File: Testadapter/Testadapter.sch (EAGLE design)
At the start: 47 parts, among them T1 C8492, T2 C8492, T3 C8545, T4 C8545, X1 MKDSN1,5/2-5,08

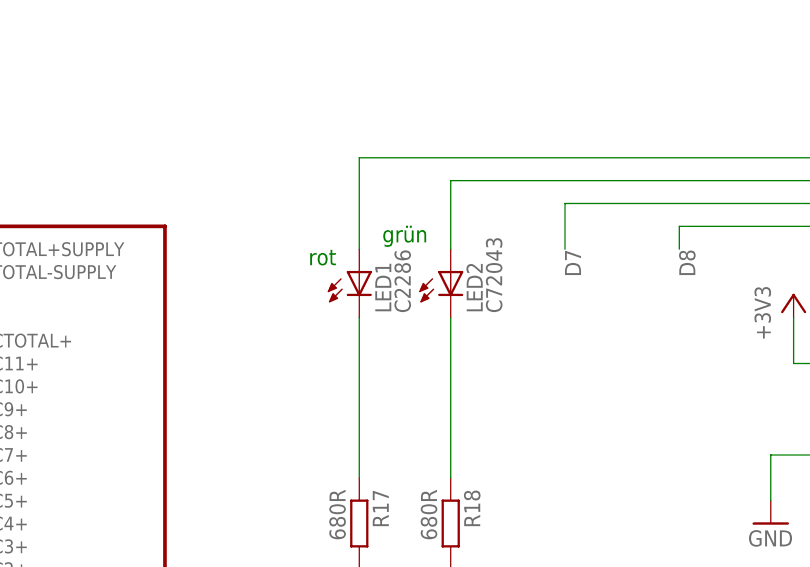
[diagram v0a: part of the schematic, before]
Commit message: apply new folder structure, renamed files, stripped EAGLE lib for MEB connectors
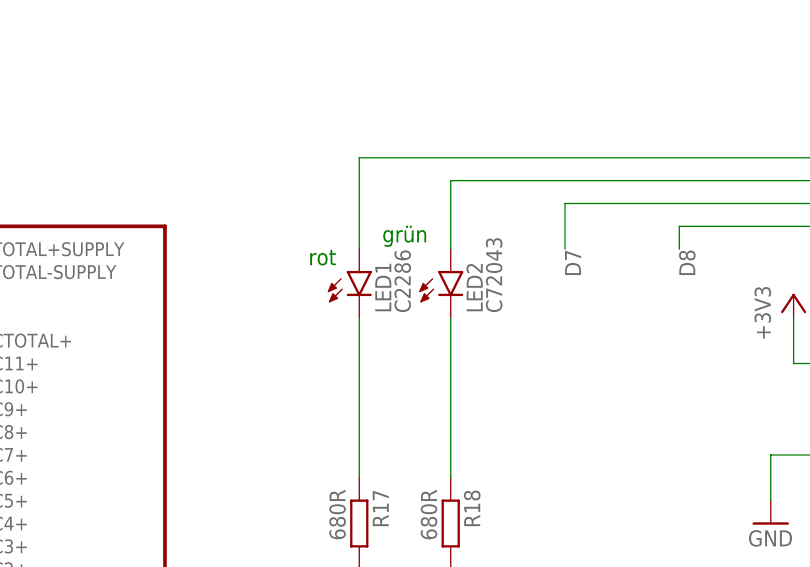
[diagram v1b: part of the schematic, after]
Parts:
- JP1: device pinhead_own:PINHD-2X11_MEB12S_MODULSEITE_SMD -> con-MEB:PINHD-2X11_MEB12S_MODULSEITE_SMD
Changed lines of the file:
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@@
 <part name="R16" library="rcl" library_urn="urn:adsk.eagle:library:334" deviceset="R-EU_" device="R0805" package3d_urn="urn:adsk.eagle:package:23553/2" value="10k"/>
 <part name="GND4" library="supply1" library_urn="urn:adsk.eagle:library:371" deviceset="GND" device=""/>
-<part name="LED1" library="led" library_urn="urn:adsk.eagle:library:259" deviceset="LED" device="CHIP-LED0603" package3d_urn="urn:adsk.eagle:package:15819/1" value="C2286"/>
-<part name="LED2" library="led" library_urn="urn:adsk.eagle:library:259" deviceset="LED" device="CHIP-LED0603" package3d_urn="urn:adsk.eagle:package:15819/1" value="C72043"/>
+<part name="LED1" library="led" library_urn="urn:adsk.eagle:library:259" deviceset="LED" device="CHIP-LED0603" package3d_urn="urn:adsk.eagle:package:15819/3" value="C2286"/>
+<part name="LED2" library="led" library_urn="urn:adsk.eagle:library:259" deviceset="LED" device="CHIP-LED0603" package3d_urn="urn:adsk.eagle:package:15819/3" value="C72043"/>
 <part name="+3V1" library="supply1" library_urn="urn:adsk.eagle:library:371" deviceset="+3V3" device=""/>
 <part name="+3V2" library="supply1" library_urn="urn:adsk.eagle:library:371" deviceset="+3V3" device=""/>
@@
 <part name="R17" library="rcl" library_urn="urn:adsk.eagle:library:334" deviceset="R-EU_" device="R0805" package3d_urn="urn:adsk.eagle:package:23553/2" value="680R"/>
 <part name="R18" library="rcl" library_urn="urn:adsk.eagle:library:334" deviceset="R-EU_" device="R0805" package3d_urn="urn:adsk.eagle:package:23553/2" value="680R"/>
-<part name="JP1" library="pinhead_own" deviceset="PINHD-2X11_MEB12S_MODULSEITE" device="_SMD"/>
+<part name="JP1" library="con-MEB" deviceset="PINHD-2X11_MEB12S_MODULSEITE" device="_SMD"/>
 <part name="GND5" library="supply1" library_urn="urn:adsk.eagle:library:371" deviceset="GND" device=""/>
 <part name="GND6" library="supply1" library_urn="urn:adsk.eagle:library:371" deviceset="GND" device=""/>
@@
 <part name="R21" library="rcl" library_urn="urn:adsk.eagle:library:334" deviceset="R-EU_" device="R0805" package3d_urn="urn:adsk.eagle:package:23553/2" value="10k"/>
 <part name="R22" library="rcl" library_urn="urn:adsk.eagle:library:334" deviceset="R-EU_" device="R0805" package3d_urn="urn:adsk.eagle:package:23553/2" value="10k"/>
-<part name="D1" library="semicon-smd-ipc" library_urn="urn:adsk.eagle:library:353" deviceset="D-FILL-" device="MLL-34" package3d_urn="urn:adsk.eagle:package:26305/1" value="C8062"/>
+<part name="D1" library="semicon-smd-ipc" library_urn="urn:adsk.eagle:library:353" deviceset="D-FILL-" device="MLL-34" package3d_urn="urn:adsk.eagle:package:26305/2" value="C8062"/>
 <part name="R23" library="rcl" library_urn="urn:adsk.eagle:library:334" deviceset="R-EU_" device="R0805" package3d_urn="urn:adsk.eagle:package:23553/2" value="10k"/>
 <part name="P+5" library="supply1" library_urn="urn:adsk.eagle:library:371" deviceset="VCC" device=""/>
@@
 <part name="R24" library="rcl" library_urn="urn:adsk.eagle:library:334" deviceset="R-EU_" device="R0805" package3d_urn="urn:adsk.eagle:package:23553/2" value="10k"/>
 <part name="R25" library="rcl" library_urn="urn:adsk.eagle:library:334" deviceset="R-EU_" device="R0805" package3d_urn="urn:adsk.eagle:package:23553/2" value="10k"/>
-<part name="D2" library="semicon-smd-ipc" library_urn="urn:adsk.eagle:library:353" deviceset="D-FILL-" device="MLL-34" package3d_urn="urn:adsk.eagle:package:26305/1" value="C8062"/>
+<part name="D2" library="semicon-smd-ipc" library_urn="urn:adsk.eagle:library:353" deviceset="D-FILL-" device="MLL-34" package3d_urn="urn:adsk.eagle:package:26305/2" value="C8062"/>
 <part name="R26" library="rcl" library_urn="urn:adsk.eagle:library:334" deviceset="R-EU_" device="R0805" package3d_urn="urn:adsk.eagle:package:23553/2" value="10k"/>
 <part name="P+6" library="supply1" library_urn="urn:adsk.eagle:library:371" deviceset="VCC" device=""/>
@@
 packages will not be understood (or retained) with this version.
 </note>
+<note version="8.4" severity="warning">
+Since Version 8.4, EAGLE supports properties for SPICE simulation.
+Probes in schematics and SPICE mapping objects found in parts and library devices
+will not be understood with this version. Update EAGLE to the latest version
+for full support of SPICE simulation.
+</note>
 </compatibility>
